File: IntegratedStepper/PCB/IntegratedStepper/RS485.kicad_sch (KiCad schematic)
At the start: 0 parts

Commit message: Add CAN circuit and edit bus from RS485 to CAN
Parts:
- added IC2: SN65HVD230DR, SOT127P600X175-8N, symbol SamacSys_Parts:SN65HVD230DR
- added R1: 10k, Resistor_SMD:R_0603_1608Metric_Pad0.98x0.95mm_HandSolder, symbol Device:R_US
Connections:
- new net: IC2.8 (RS), R1.1
- new net 3V3: IC2.3 (VCC)
- new net CANH: IC2.6 (CANL)
- new net CANL: IC2.7 (CANH)
- new net GND: IC2.2 (GND), R1.2
- new net RX: IC2.4 (R)
- new net TX: IC2.1 (D)
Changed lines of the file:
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@@
 (kicad_sch (version 20230121) (generator eeschema)
   (paper "A4")
+  (wire (pts (xy 160.02 88.9) (xy 166.37 88.9))
+    (stroke (width 0) (type default))
+  )
+  (wire (pts (xy 121.92 88.9) (xy 132.08 88.9))
+    (stroke (width 0) (type default))
+  )
+  (wire (pts (xy 125.73 91.44) (xy 132.08 91.44))
+    (stroke (width 0) (type default))
+  )
+  (wire (pts (xy 125.73 86.36) (xy 132.08 86.36))
+    (stroke (width 0) (type default))
+  )
+  (wire (pts (xy 160.02 93.98) (xy 163.83 93.98))
+    (stroke (width 0) (type default))
+  )
+  (wire (pts (xy 125.73 93.98) (xy 132.08 93.98))
+    (stroke (width 0) (type default))
+  )
+  (wire (pts (xy 163.83 101.6) (xy 163.83 105.41))
+    (stroke (width 0) (type default))
+  )
+  (wire (pts (xy 160.02 91.44) (xy 166.37 91.44))
+    (stroke (width 0) (type default))
+  )
+  (hierarchical_label "TX" (shape input) (at 125.73 86.36 180) (fields_autoplaced)
+    (effects (font (size 1.27 1.27)) (justify right))
+  )
+  (hierarchical_label "RX" (shape input) (at 125.73 93.98 180) (fields_autoplaced)
+    (effects (font (size 1.27 1.27)) (justify right))
+  )
+  (hierarchical_label "CANL" (shape input) (at 166.37 91.44 0) (fields_autoplaced)
+    (effects (font (size 1.27 1.27)) (justify left))
+  )
+  (hierarchical_label "CANH" (shape input) (at 166.37 88.9 0) (fields_autoplaced)
+    (effects (font (size 1.27 1.27)) (justify left))
+  )
+  (hierarchical_label "3V3" (shape input) (at 125.73 91.44 180) (fields_autoplaced)
+    (effects (font (size 1.27 1.27)) (justify right))
+  )
+  (symbol (lib_id "Device:R_US") (at 163.83 97.79 0) (unit 1)
+    (in_bom yes) (on_board yes) (dnp no) (fields_autoplaced)
+    (property "Reference" "R1" (at 166.37 97.155 0)
+      (effects (font (size 1.27 1.27)) (justify left))
+    )
+    (property "Value" "10k" (at 166.37 99.695 0)
+      (effects (font (size 1.27 1.27)) (justify left))
+    )
+    (property "Footprint" "Resistor_SMD:R_0603_1608Metric_Pad0.98x0.95mm_HandSolder" (at 164.846 98.044 90)
+      (effects (font (size 1.27 1.27)) hide)
+    )
+    (property "Datasheet" "~" (at 163.83 97.79 0)
+      (effects (font (size 1.27 1.27)) hide)
+    )
+    (pin "1")
+    (pin "2")
+    (instances
+      (project "IntegratedStepper"
+        (path "/ab592993-dafc-411a-b466-8e8425f43767/f6cdbece-6675-4a06-843f-4c3f5c22b49a"
+          (reference "R1") (unit 1)
+        )
+      )
+    )
+  )
+  (symbol (lib_id "SamacSys_Parts:SN65HVD230DR") (at 132.08 86.36 0) (unit 1)
+    (in_bom yes) (on_board yes) (dnp no) (fields_autoplaced)
+    (property "Reference" "IC2" (at 146.05 80.01 0)
+      (effects (font (size 1.27 1.27)))
+    )
+    (property "Value" "SN65HVD230DR" (at 146.05 82.55 0)
+      (effects (font (size 1.27 1.27)))
+    )
+    (property "Footprint" "SOT127P600X175-8N" (at 156.21 83.82 0)
+      (effects (font (size 1.27 1.27)) (justify left) hide)
+    )
+    (property "Datasheet" "http://www.ti.com/lit/gpn/sn65hvd230" (at 156.21 86.36 0)
+      (effects (font (size 1.27 1.27)) (justify left) hide)
+    )
+    (property "Description" "3.3 V CAN Transceiver with Standby Mode" (at 156.21 88.9 0)
+      (effects (font (size 1.27 1.27)) (justify left) hide)
+    )
+    (property "Height" "1.75" (at 156.21 91.44 0)
+      (effects (font (size 1.27 1.27)) (justify left) hide)
+    )
+    (property "Mouser Part Number" "595-SN65HVD230DR" (at 156.21 93.98 0)
+      (effects (font (size 1.27 1.27)) (justify left) hide)
+    )
+    (property "Mouser Price/Stock" "https://www.mouser.co.uk/ProductDetail/Texas-Instruments/SN65HVD230DR?qs=QViXGNcIEAtifeQR3pYVUQ%3D%3D" (at 156.21 96.52 0)
+      (effects (font (size 1.27 1.27)) (justify left) hide)
+    )
+    (property "Manufacturer_Name" "Texas Instruments" (at 156.21 99.06 0)
+      (effects (font (size 1.27 1.27)) (justify left) hide)
+    )
+    (property "Manufacturer_Part_Number" "SN65HVD230DR" (at 156.21 101.6 0)
+      (effects (font (size 1.27 1.27)) (justify left) hide)
+    )
+    (pin "1")
+    (pin "2")
+    (pin "3")
+    (pin "4")
+    (pin "5")
+    (pin "6")
+    (pin "7")
+    (pin "8")
+    (instances
+      (project "IntegratedStepper"
+        (path "/ab592993-dafc-411a-b466-8e8425f43767/f6cdbece-6675-4a06-843f-4c3f5c22b49a"
+          (reference "IC2") (unit 1)
+        )
+      )
+    )
+  )
+  (symbol (lib_id "power:GND") (at 121.92 88.9 270) (unit 1)
+    (in_bom yes) (on_board yes) (dnp no) (fields_autoplaced)
+    (property "Reference" "#PWR06" (at 115.57 88.9 0)
+      (effects (font (size 1.27 1.27)) hide)
+    )
+    (property "Value" "GND" (at 118.11 89.535 90)
+      (effects (font (size 1.27 1.27)) (justify right))
+    )
+    (property "Footprint" "" (at 121.92 88.9 0)
+      (effects (font (size 1.27 1.27)) hide)
+    )
+    (property "Datasheet" "" (at 121.92 88.9 0)
+      (effects (font (size 1.27 1.27)) hide)
+    )
+    (pin "1")
+    (instances
+      (project "IntegratedStepper"
+        (path "/ab592993-dafc-411a-b466-8e8425f43767/f6cdbece-6675-4a06-843f-4c3f5c22b49a"
+          (reference "#PWR06") (unit 1)
+        )
+      )
+    )
+  )
+  (symbol (lib_id "power:GND") (at 163.83 105.41 0) (unit 1)
+    (in_bom yes) (on_board yes) (dnp no) (fields_autoplaced)
+    (property "Reference" "#PWR07" (at 163.83 111.76 0)
+      (effects (font (size 1.27 1.27)) hide)
+    )
+    (property "Value" "GND" (at 163.83 110.49 0)
+      (effects (font (size 1.27 1.27)))
+    )
+    (property "Footprint" "" (at 163.83 105.41 0)
+      (effects (font (size 1.27 1.27)) hide)
+    )
+    (property "Datasheet" "" (at 163.83 105.41 0)
+      (effects (font (size 1.27 1.27)) hide)
+    )
+    (pin "1")
+    (instances
+      (project "IntegratedStepper"
+        (path "/ab592993-dafc-411a-b466-8e8425f43767/f6cdbece-6675-4a06-843f-4c3f5c22b49a"
+          (reference "#PWR07") (unit 1)
+        )
+      )
+    )
+  )
 )

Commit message: update Vreg for Integrated Stepper
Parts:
- IC2: footprint SOT127P600X175-8N -> SamacSys_Parts:SOT127P600X175-8N
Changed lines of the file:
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@@
       (effects (font (size 1.27 1.27)))
     )
-    (property "Footprint" "SOT127P600X175-8N" (at 156.21 83.82 0)
+    (property "Footprint" "SamacSys_Parts:SOT127P600X175-8N" (at 156.21 83.82 0)
       (effects (font (size 1.27 1.27)) (justify left) hide)
     )

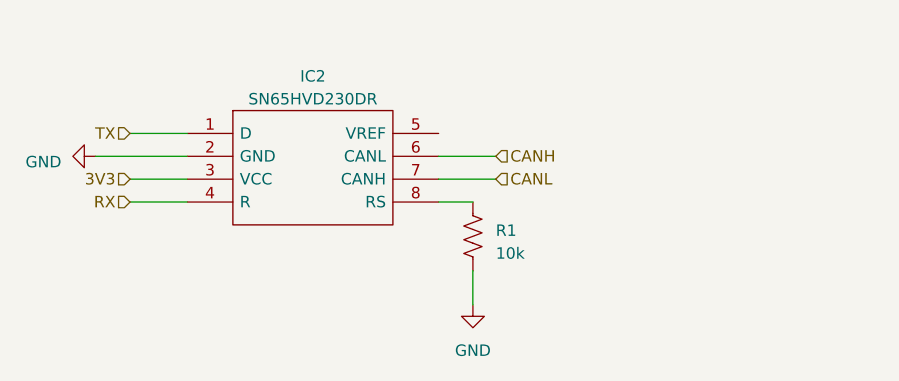
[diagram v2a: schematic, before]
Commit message: Update Integrated Stepper PCB with ESP sch and CAN sch
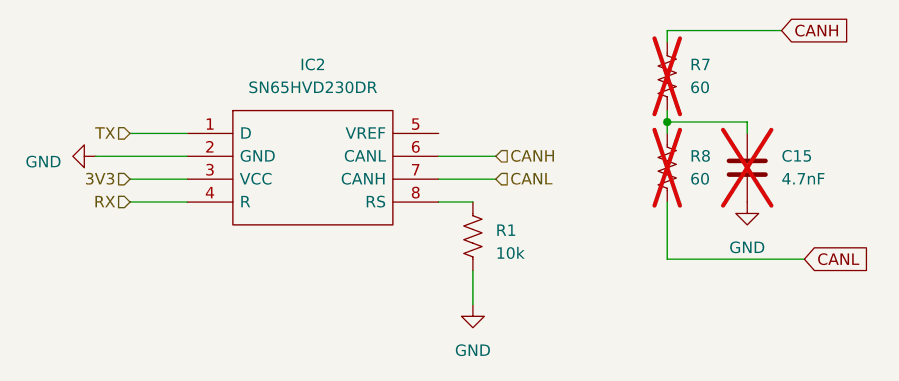
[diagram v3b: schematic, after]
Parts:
- added C15: 4.7nF, Capacitor_SMD:C_0603_1608Metric, symbol Device:C
- added R7, R8: 60, Resistor_SMD:R_0603_1608Metric, symbol Device:R_US
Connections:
- net CANH: now also R7.1
- net CANL: now also R8.2
- net GND: now also C15.2
- new net: C15.1, R7.2, R8.1

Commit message: Update Integrated Stepper with inital PCB
This is going to be so hard :(
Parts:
- R1: footprint Resistor_SMD:R_0603_1608Metric_Pad0.98x0.95mm_HandSolder -> Resistor_SMD:R_0603_1608Metric
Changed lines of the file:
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@@
 			)
 		)
-		(property "Footprint" "Resistor_SMD:R_0603_1608Metric_Pad0.98x0.95mm_HandSolder"
+		(property "Footprint" "Resistor_SMD:R_0603_1608Metric"
 			(at 164.846 98.044 90)
 			(effects

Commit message: Add intermediate layout + routing to integrated stepper
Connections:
- net RX renamed CAN_RX
- net TX renamed CAN_TX
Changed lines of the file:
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@@
 		)
 	)
-	(hierarchical_label "TX"
+	(hierarchical_label "CAN_TX"
 		(shape input)
 		(at 125.73 86.36 180)
@@
 		)
 	)
-	(hierarchical_label "RX"
+	(hierarchical_label "CAN_RX"
 		(shape input)
 		(at 125.73 93.98 180)

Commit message: add changes for instock parts
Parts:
- R1: LCSC (none) -> C469659; LCSC Part (none) -> C469659; LCSC Part Number (none) -> C469659
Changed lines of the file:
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@@
+			)
+		)
+		(property "LCSC" "C469659"
+			(at 163.83 97.79 0)
+			(effects
+				(font
+					(size 1.27 1.27)
+				)
+				(hide yes)
+			)
+		)
+		(property "LCSC Part" "C469659"
+			(at 163.83 97.79 0)
+			(effects
+				(font
+					(size 1.27 1.27)
+				)
+				(hide yes)
+			)
+		)
+		(property "LCSC Part Number" "C469659"
+			(at 163.83 97.79 0)
+			(effects
+				(font
+					(size 1.27 1.27)
+				)
+				(hide yes)
 			)
 		)

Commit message: update with more in stock parts
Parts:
- C15: LCSC (none) -> C2929200; LCSC Part (none) -> C2929200; LCSC Part Number (none) -> C2929200
- IC2: LCSC (none) -> C12084; LCSC Part (none) -> C12084; LCSC Part Number (none) -> C12084
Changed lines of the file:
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@@
+			)
+		)
+		(property "Voltage Rating" ""
+			(at 194.31 90.17 0)
+			(effects
+				(font
+					(size 1.27 1.27)
+				)
+				(hide yes)
+			)
+		)
+		(property "LCSC" "C2929200"
+			(at 194.31 90.17 0)
+			(effects
+				(font
+					(size 1.27 1.27)
+				)
+				(hide yes)
+			)
+		)
+		(property "LCSC Part Number" "C2929200"
+			(at 194.31 90.17 0)
+			(effects
+				(font
+					(size 1.27 1.27)
+				)
+				(hide yes)
+			)
+		)
+		(property "LCSC Part" "C2929200"
+			(at 194.31 90.17 0)
+			(effects
+				(font
+					(size 1.27 1.27)
+				)
+				(hide yes)
 			)
 		)
@@
 				(hide yes)
 			)
+		)
+		(property "LCSC" "C12084"
+			(at 132.08 86.36 0)
+			(effects
+				(font
+					(size 1.27 1.27)
+				)
+				(hide yes)
+			)
+		)
+		(property "LCSC Part" "C12084"
+			(at 132.08 86.36 0)
+			(effects
+				(font
+					(size 1.27 1.27)
+				)
+				(hide yes)
+			)
+		)
+		(property "LCSC Part Number" "C12084"
+			(at 132.08 86.36 0)
+			(effects
+				(font
+					(size 1.27 1.27)
+				)
+				(hide yes)
+			)
